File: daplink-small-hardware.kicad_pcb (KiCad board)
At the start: 4 copper layers, 34 x 15.2 mm, 46 parts, among them J1 Pin_SWD_FIRMWARE, J2 USB_C_Receptacle_USB2.0, J4 Conn_SWD, J5 Conn_UART, Q1 S8050-SOT23, U1 STM32F103CBTx, U2 RS3236-3.3, Y1 Crystal_GND24

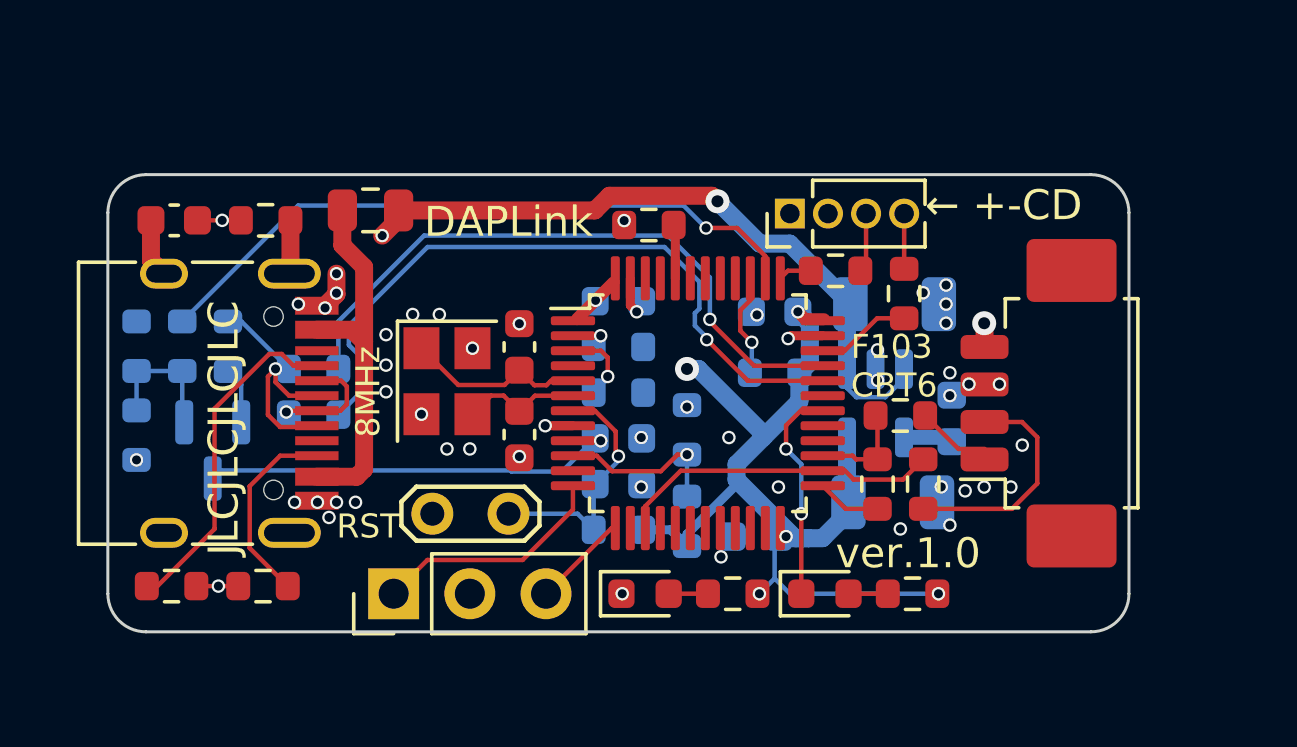
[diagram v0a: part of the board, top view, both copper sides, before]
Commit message: Add esd protection; ->Ver1.0.1
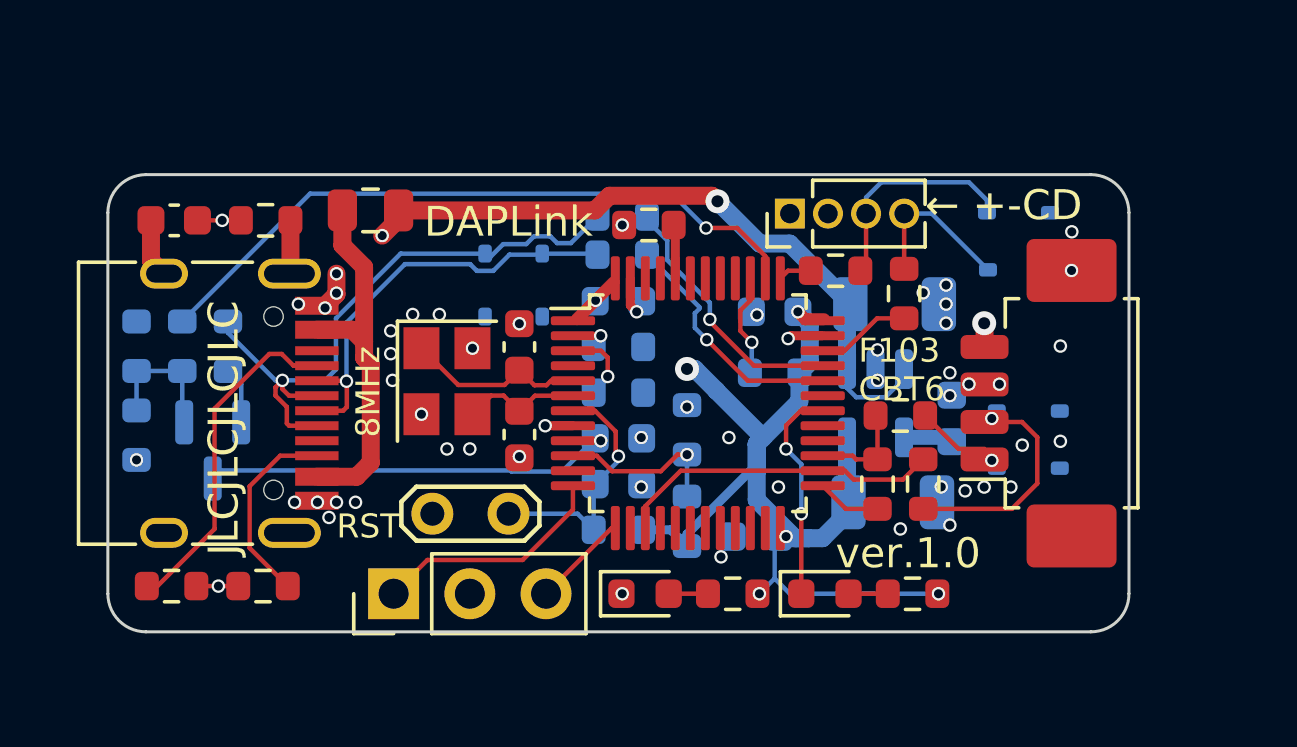
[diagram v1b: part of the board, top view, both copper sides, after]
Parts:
- added D3: ESD9B3.3ST5G, Diode_SMD:D_SOD-323, B.Cu at (158.9, 85.0)
- added D4: ESD9B3.3ST5G, Diode_SMD:D_SOD-323, B.Cu at (157.0, 85.0)
- added D5: ESD9B3.3ST5G, Diode_SMD:D_SOD-323, B.Cu at (174.8, 84.5)
- added D6: ESD9B3.3ST5G, Diode_SMD:D_SOD-323, B.Cu at (174.8, 82.5)
- added D7: ESD9B3.3ST5G, Diode_SMD:D_SOD-323, B.Cu at (175.1, 91.1)
- added D8: ESD9B3.3ST5G, Diode_SMD:D_SOD-323, B.Cu at (175.1, 89.2)
- moved R11 11.6 mm to (161.5, 83.9)
- moved R12 11.5 mm to (161.5, 82.7)
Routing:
- net /STL_USB_DM: track 23.2 -> 8.22 mm
- net /STL_USB_DP: track 21.6 -> 8.74 mm
- net Net-(D4-A1): track 8.59 -> 21.2 mm
- net Net-(D3-A1): track 3.80 -> 14.5 mm
- net /ST_SWCLK: track 1.98 -> 7.42 mm
- net /ST_SWDIO: track 1.84 -> 5.41 mm
- net +3V3: track 75.0 -> 75.5 mm
- net Net-(D8-A1): track 7.66 -> 7.76 mm, vias 0 -> 1
- net Net-(D7-A1): vias 0 -> 1
- net GND: vias 51 -> 55
